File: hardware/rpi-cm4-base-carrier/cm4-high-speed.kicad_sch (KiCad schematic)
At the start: 1 part

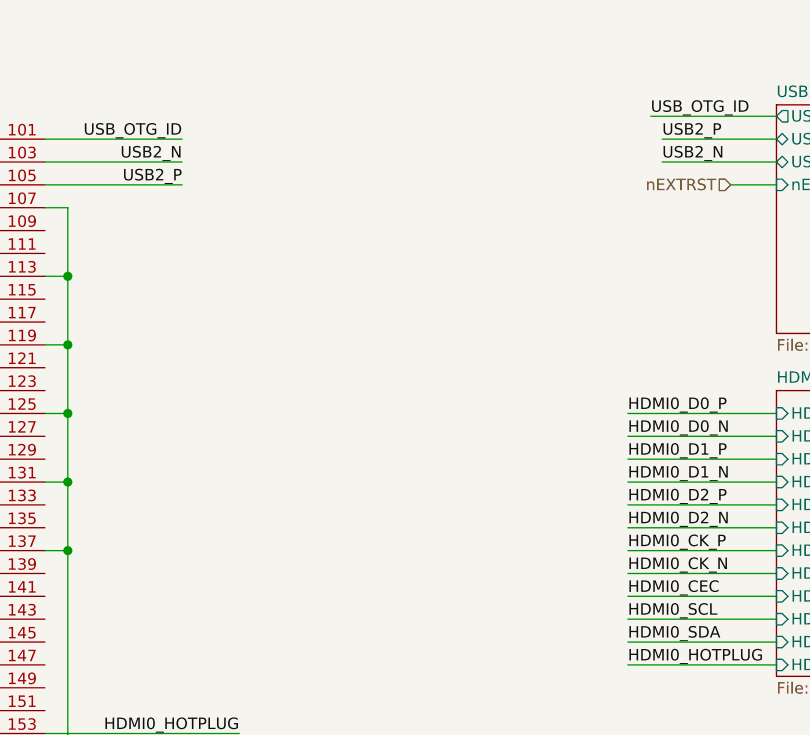
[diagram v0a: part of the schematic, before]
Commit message: routing for some modules progressing quickly, USBHUB mostly complete, thought needed regarding which connectors should be exposed post assembly and which should be for internal use only. LED identifiers and buttons still missing
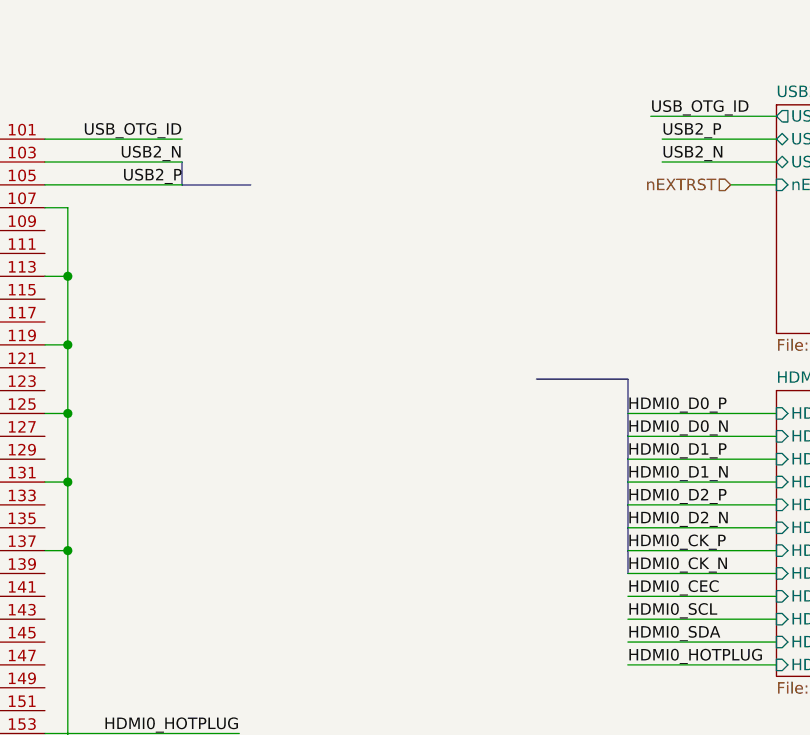
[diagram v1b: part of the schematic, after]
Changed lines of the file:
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@@
     (stroke (width 0) (type solid))
+  )
+  (bus (pts (xy 119.38 50.8) (xy 127 50.8))
+    (stroke (width 0) (type default))
   )
   (wire (pts (xy 40.64 137.16) (xy 43.18 137.16))
@@
     (stroke (width 0) (type solid))
   )
+  (bus (pts (xy 168.91 72.39) (xy 168.91 93.98))
+    (stroke (width 0) (type default))
+  )
   (wire (pts (xy 104.14 160.02) (xy 106.68 160.02))
     (stroke (width 0) (type solid))
@@
     (stroke (width 0) (type solid))
   )
+  (bus (pts (xy 119.38 48.26) (xy 119.38 50.8))
+    (stroke (width 0) (type default))
+  )
   (wire (pts (xy 40.64 160.02) (xy 43.18 160.02))
     (stroke (width 0) (type solid))
+  )
+  (bus (pts (xy 158.75 72.39) (xy 168.91 72.39))
+    (stroke (width 0) (type default))
   )
   (wire (pts (xy 40.64 121.92) (xy 43.18 121.92))
@@
     (effects (font (size 1.27 1.27)) (justify right))
   )
+  (netclass_flag "" (length 2.54) (shape round) (at 158.75 72.39 0) (fields_autoplaced)
+    (effects (font (size 1.27 1.27)) (justify left bottom))
+    (property "Netclass" "HDMI 100R Diff" (at 159.639 69.85 0)
+      (effects (font (size 1.27 1.27) italic) (justify left))
+    )
+  )
+  (netclass_flag "" (length 2.54) (shape round) (at 127 50.8 0) (fields_autoplaced)
+    (effects (font (size 1.27 1.27)) (justify left bottom))
+    (property "Netclass" "USB 90R Diff" (at 127.889 48.26 0)
+      (effects (font (size 1.27 1.27) italic) (justify left))
+    )
+  )
   (symbol (lib_id "power:GND") (at 40.64 175.26 0) (unit 1)
     (in_bom yes) (on_board yes) (dnp no)
-    (property "Reference" "#PWR0111" (at 40.64 181.61 0)
+    (property "Reference" "#PWR015" (at 40.64 181.61 0)
       (effects (font (size 1.27 1.27)) hide)
     )
@@
       (project "rpi-cm4-base-carrier"
         (path "/92c58705-ecb0-498b-b561-44a3f0daad57/caa71f4c-454d-4ac9-b287-456eafb34991"
-          (reference "#PWR0111") (unit 1)
+          (reference "#PWR015") (unit 1)
         )
       )
@@
   (symbol (lib_id "power:GND") (at 106.68 175.26 0) (unit 1)
     (in_bom yes) (on_board yes) (dnp no)
-    (property "Reference" "#PWR0112" (at 106.68 181.61 0)
+    (property "Reference" "#PWR016" (at 106.68 181.61 0)
       (effects (font (size 1.27 1.27)) hide)
     )
@@
       (project "rpi-cm4-base-carrier"
         (path "/92c58705-ecb0-498b-b561-44a3f0daad57/caa71f4c-454d-4ac9-b287-456eafb34991"
-          (reference "#PWR0112") (unit 1)
+          (reference "#PWR016") (unit 1)
         )
       )

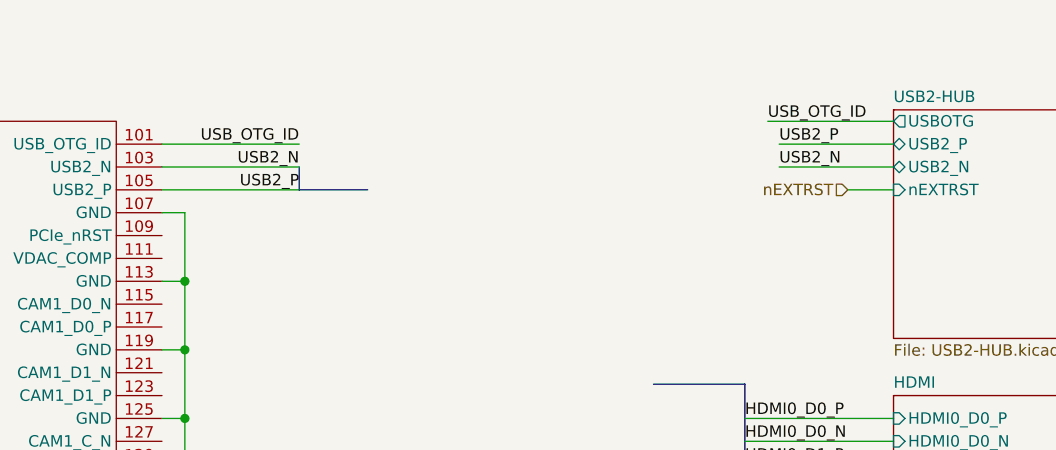
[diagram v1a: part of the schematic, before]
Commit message: started final placement of blocks, realised ESD suppression devices cannot be manufactured with JLC, need to switch part
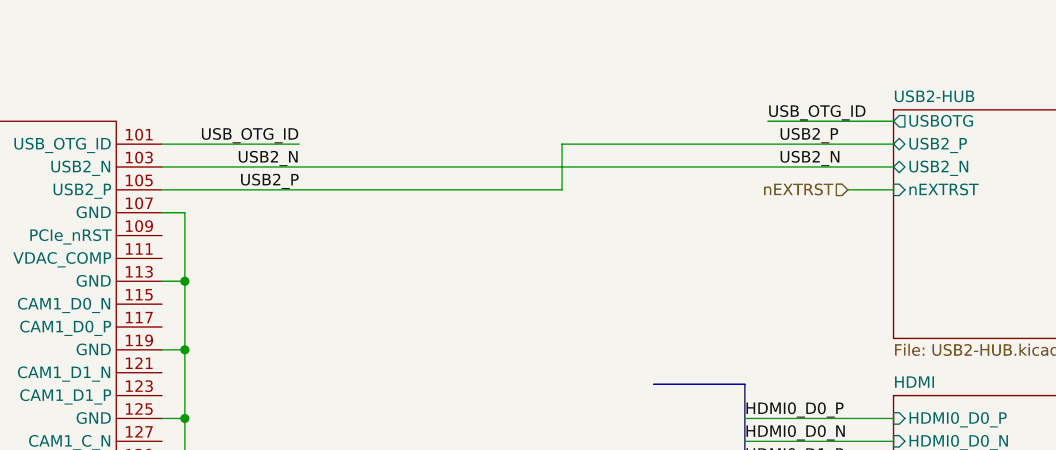
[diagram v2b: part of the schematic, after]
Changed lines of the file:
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@@
     (stroke (width 0) (type solid))
-  )
-  (bus (pts (xy 119.38 50.8) (xy 127 50.8))
-    (stroke (width 0) (type default))
   )
   (wire (pts (xy 40.64 137.16) (xy 43.18 137.16))
@@
     (stroke (width 0) (type solid))
   )
-  (wire (pts (xy 172.72 45.72) (xy 185.42 45.72))
+  (wire (pts (xy 148.59 45.72) (xy 185.42 45.72))
     (stroke (width 0) (type solid))
   )
@@
     (stroke (width 0) (type solid))
   )
+  (wire (pts (xy 148.59 50.8) (xy 148.59 45.72))
+    (stroke (width 0) (type solid))
+  )
   (wire (pts (xy 104.14 144.78) (xy 106.68 144.78))
     (stroke (width 0) (type solid))
@@
     (stroke (width 0) (type solid))
   )
-  (wire (pts (xy 104.14 50.8) (xy 119.38 50.8))
-    (stroke (width 0) (type solid))
-  )
-  (bus (pts (xy 119.38 48.26) (xy 119.38 50.8))
-    (stroke (width 0) (type default))
+  (wire (pts (xy 104.14 50.8) (xy 148.59 50.8))
+    (stroke (width 0) (type solid))
   )
   (wire (pts (xy 40.64 160.02) (xy 43.18 160.02))
@@
     (stroke (width 0) (type solid))
   )
-  (wire (pts (xy 104.14 48.26) (xy 119.38 48.26))
-    (stroke (width 0) (type solid))
-  )
   (wire (pts (xy 106.68 53.34) (xy 106.68 60.96))
     (stroke (width 0) (type solid))
@@
     (stroke (width 0) (type solid))
   )
+  (wire (pts (xy 104.14 48.26) (xy 185.42 48.26))
+    (stroke (width 0) (type default))
+  )
   (wire (pts (xy 168.91 83.82) (xy 185.42 83.82))
     (stroke (width 0) (type solid))
@@
   (wire (pts (xy 40.64 91.44) (xy 40.64 99.06))
     (stroke (width 0) (type solid))
-  )
-  (wire (pts (xy 172.72 48.26) (xy 185.42 48.26))
-    (stroke (width 0) (type default))
   )
   (wire (pts (xy 106.68 129.54) (xy 106.68 137.16))
@@
     (effects (font (size 1.27 1.27)) (justify right))
   )
+  (netclass_flag "" (length 2.54) (shape round) (at 133.35 48.26 0) (fields_autoplaced)
+    (effects (font (size 1.27 1.27)) (justify left bottom))
+    (property "Netclass" "USB 90R Diff" (at 134.239 45.72 0)
+      (effects (font (size 1.27 1.27) italic) (justify left))
+    )
+  )
   (netclass_flag "" (length 2.54) (shape round) (at 158.75 72.39 0) (fields_autoplaced)
     (effects (font (size 1.27 1.27)) (justify left bottom))
@@
     )
   )
-  (netclass_flag "" (length 2.54) (shape round) (at 127 50.8 0) (fields_autoplaced)
-    (effects (font (size 1.27 1.27)) (justify left bottom))
-    (property "Netclass" "USB 90R Diff" (at 127.889 48.26 0)
+  (netclass_flag "" (length 2.54) (shape round) (at 148.59 45.72 0) (fields_autoplaced)
+    (effects (font (size 1.27 1.27)) (justify left bottom))
+    (property "Netclass" "USB 90R Diff" (at 149.479 43.18 0)
       (effects (font (size 1.27 1.27) italic) (justify left))
     )
@@
   (symbol (lib_id "power:GND") (at 40.64 175.26 0) (unit 1)
     (in_bom yes) (on_board yes) (dnp no)
-    (property "Reference" "#PWR015" (at 40.64 181.61 0)
+    (property "Reference" "#PWR014" (at 40.64 181.61 0)
       (effects (font (size 1.27 1.27)) hide)
     )
@@
     )
     (property "Datasheet" "" (at 40.64 175.26 0)
+      (effects (font (size 1.27 1.27)) hide)
+    )
+    (pin "1")
+    (instances
+      (project "rpi-cm4-base-carrier"
+        (path "/92c58705-ecb0-498b-b561-44a3f0daad57/caa71f4c-454d-4ac9-b287-456eafb34991"
+          (reference "#PWR014") (unit 1)
+        )
+      )
+    )
+  )
+  (symbol (lib_id "power:GND") (at 106.68 175.26 0) (unit 1)
+    (in_bom yes) (on_board yes) (dnp no)
+    (property "Reference" "#PWR015" (at 106.68 181.61 0)
+      (effects (font (size 1.27 1.27)) hide)
+    )
+    (property "Value" "GND" (at 107.95 180.34 0)
+      (effects (font (size 1.27 1.27)))
+    )
+    (property "Footprint" "" (at 106.68 175.26 0)
+      (effects (font (size 1.27 1.27)) hide)
+    )
+    (property "Datasheet" "" (at 106.68 175.26 0)
       (effects (font (size 1.27 1.27)) hide)
     )
@@
         )
       )
-    )
-  )
-  (symbol (lib_id "power:GND") (at 106.68 175.26 0) (unit 1)
-    (in_bom yes) (on_board yes) (dnp no)
-    (property "Reference" "#PWR016" (at 106.68 181.61 0)
-      (effects (font (size 1.27 1.27)) hide)
-    )
-    (property "Value" "GND" (at 107.95 180.34 0)
-      (effects (font (size 1.27 1.27)))
-    )
-    (property "Footprint" "" (at 106.68 175.26 0)
-      (effects (font (size 1.27 1.27)) hide)
-    )
-    (property "Datasheet" "" (at 106.68 175.26 0)
-      (effects (font (size 1.27 1.27)) hide)
-    )
-    (pin "1")
-    (instances
-      (project "rpi-cm4-base-carrier"
-        (path "/92c58705-ecb0-498b-b561-44a3f0daad57/caa71f4c-454d-4ac9-b287-456eafb34991"
-          (reference "#PWR016") (unit 1)
-        )
-      )

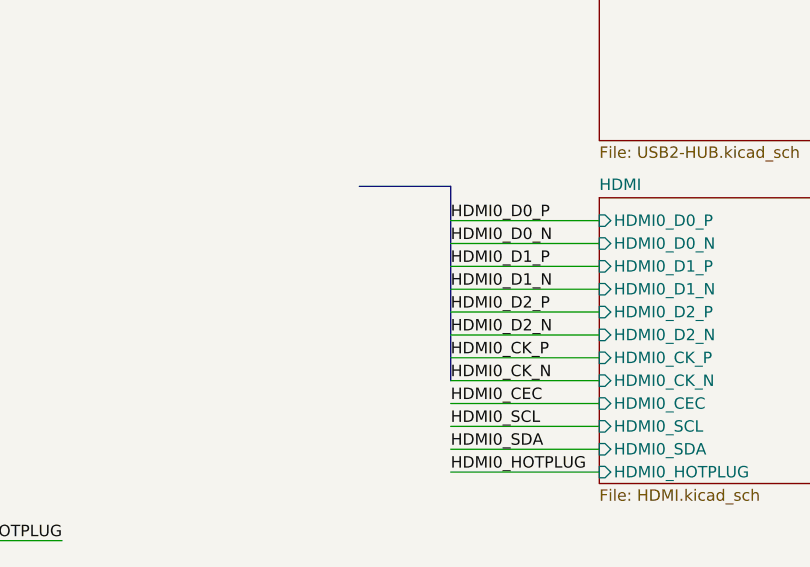
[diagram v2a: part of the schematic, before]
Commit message: most diff pairs routed, forgot about intra-pair spacing
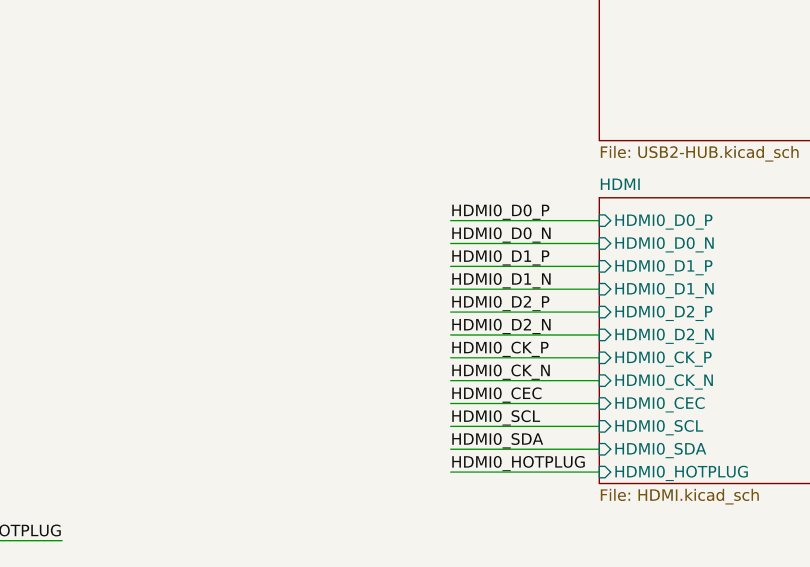
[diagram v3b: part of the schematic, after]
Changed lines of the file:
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@@
     (stroke (width 0) (type solid))
-  )
-  (bus (pts (xy 168.91 72.39) (xy 168.91 93.98))
-    (stroke (width 0) (type default))
   )
   (wire (pts (xy 104.14 160.02) (xy 106.68 160.02))
@@
   (wire (pts (xy 40.64 160.02) (xy 43.18 160.02))
     (stroke (width 0) (type solid))
-  )
-  (bus (pts (xy 158.75 72.39) (xy 168.91 72.39))
-    (stroke (width 0) (type default))
   )
   (wire (pts (xy 40.64 121.92) (xy 43.18 121.92))
@@
       (effects (font (size 1.27 1.27) italic) (justify left))
     )
-  )
-  (netclass_flag "" (length 2.54) (shape round) (at 158.75 72.39 0) (fields_autoplaced)
-    (effects (font (size 1.27 1.27)) (justify left bottom))
-    (property "Netclass" "HDMI 100R Diff" (at 159.639 69.85 0)
-      (effects (font (size 1.27 1.27) italic) (justify left))
-    )

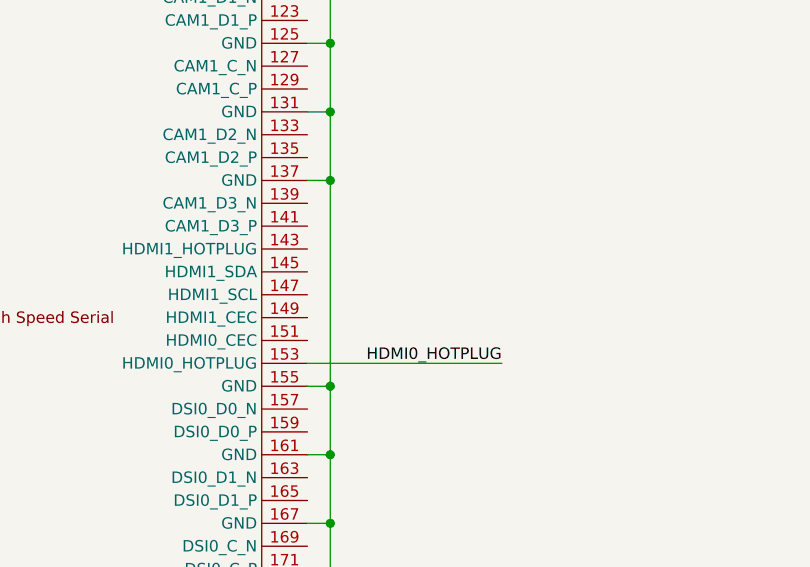
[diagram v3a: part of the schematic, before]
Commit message: schematic entry for samtec board edge connector complete, started breakout of GPIO lines for connection to board edge connector
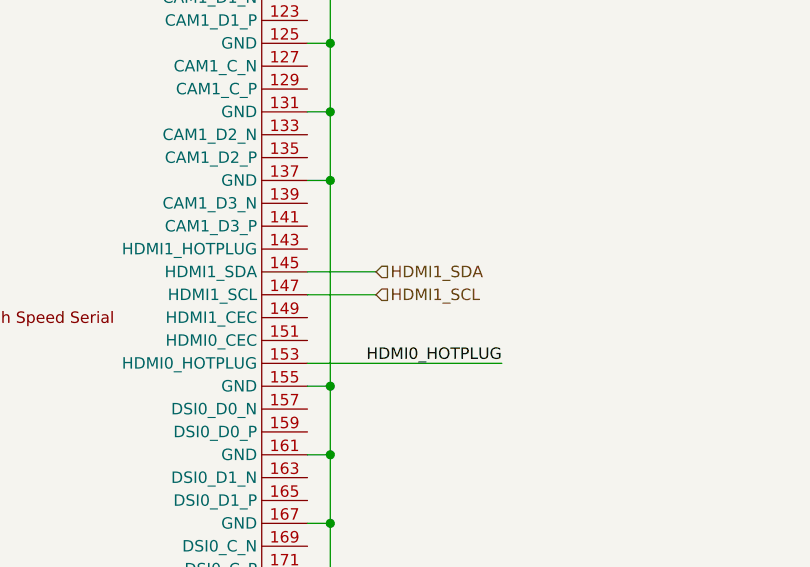
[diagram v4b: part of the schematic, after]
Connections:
- net HDMI1_SDA: now reaches Module1.145 (HDMI1_SDA)
- net HDMI1_SCL: now reaches Module1.147 (HDMI1_SCL)
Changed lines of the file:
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@@
     (stroke (width 0) (type solid))
+  )
+  (wire (pts (xy 104.14 104.14) (xy 111.76 104.14))
+    (stroke (width 0) (type default))
   )
   (wire (pts (xy 104.14 160.02) (xy 106.68 160.02))
@@
   (wire (pts (xy 106.68 83.82) (xy 106.68 91.44))
     (stroke (width 0) (type solid))
+  )
+  (wire (pts (xy 104.14 101.6) (xy 111.76 101.6))
+    (stroke (width 0) (type default))
   )
   (wire (pts (xy 180.34 50.8) (xy 185.42 50.8))
@@
     (effects (font (size 1.27 1.27)) (justify right))
   )
+  (hierarchical_label "HDMI1_SCL" (shape input) (at 111.76 104.14 0) (fields_autoplaced)
+    (effects (font (size 1.27 1.27)) (justify left))
+  )
+  (hierarchical_label "HDMI1_SDA" (shape input) (at 111.76 101.6 0) (fields_autoplaced)
+    (effects (font (size 1.27 1.27)) (justify left))
+  )
   (netclass_flag "" (length 2.54) (shape round) (at 133.35 48.26 0) (fields_autoplaced)

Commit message: design files exported ready for manufacture, LCSC part numbers added throughout the library
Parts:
- Module1: LCSC Part # (none) -> C597931; LCSC Part Number (none) -> C597931
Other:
- title: Raspberry Pi Compute Module 4 Base Carrier -> Raspberry Pi Compute Module 4 Control Node
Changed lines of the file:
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@@
   (paper "A4")
   (title_block
-    (title "Raspberry Pi Compute Module 4 Base Carrier")
-    (date "2020-10-31")
+    (title "Raspberry Pi Compute Module 4 Control Node")
+    (date "2024-02-04")
     (rev "v01")
-    (comment 2 "creativecommons.org/licenses/by-sa/4.0")
+    (comment 2 "creativecommons.org/licenses/by-sa/4.0/")
     (comment 3 "License: CC BY-SA 4.0")
-    (comment 4 "Author: Shawn Hymel")
+    (comment 4 "Author: Sam Earnshaw")
   )
   (junction (at 40.64 106.68) (diameter 1.016) (color 0 0 0 0)
@@
       (effects (font (size 1.27 1.27)) hide)
     )
+    (property "LCSC Part Number" "C597931" (at -66.04 106.68 0)
+      (effects (font (size 1.27 1.27)) hide)
+    )
+    (property "LCSC Part #" "C597931" (at -66.04 106.68 0)
+      (effects (font (size 1.27 1.27)) hide)
+    )
